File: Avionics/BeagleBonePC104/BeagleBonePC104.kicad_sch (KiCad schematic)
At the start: 5 parts

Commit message: Ian Goldberg - Finished the footprint for the BeagleBonePCI104 Motherboard
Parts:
- removed U2: ~, symbol PCI104:PCI104Connector
- removed U3: ~, AdafruitCANTransciever:AdafruitCANPal_TJA1051T, symbol BeagleBoneBlackPinout:AdafruitCANTransciever
- added U2: ~, PCI104Connector:PCI104ConnectorAttempt#2H1, symbol PCI104:PCI104H1
- added U3: ~, AdafruitCANTransciever:AdafruitCANPal_TJA1051T, symbol BeagleBoneBlackPinout:AdafruitCANTranscieverAttempt#2
- added U4: ~, PCI104Connector:PCI104ConnectorAttempt#2H2, symbol PCI104:PCI104H2
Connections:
- net GPIO3_21 is gone; now on net CAN_SLNT: U1.25 (GPIO3_21)
- net 3V3: now also U2.25 (3V3_MAIN), U2.26 (3V3_MAIN), U3.1 (Vcc), U4.27 (3V3_MAIN), U4.28 (3V3_MAIN)
- net 5V: now also U4.25 (5V_MAIN), U4.26 (5V_MAIN)
- net CAN1_RX: now also U3.4 (TX)
- net CAN1_TX: now also U3.3 (RX)
- net CAN_H: now also U2.3 (CANH1), U3.6 (CANH)
- net CAN_L: now also U2.1 (CANL1), U3.7 (CANL)
- net GND: now also U3.2 (GND), U4.29 (GND), U4.30 (GND), U4.31 (GND), U4.32 (GND)
- net GPI02_22: now also U2.29
- net GPIO0_7: now also U4.19
- net GPIO1_12: now also U2.13
- net GPIO1_13: now also U2.11
- net GPIO1_14: now also U4.17
- net GPIO1_15: now also U2.17
- net GPIO1_16: now also U4.40
- net GPIO1_17: now also U4.44
- net GPIO1_26: now also U2.15
- net GPIO1_27: now also U2.21
- net GPIO1_28: now also U4.43
- net GPIO1_29: now also U2.27
- net GPIO2_1: now also U2.23
- net GPIO2_10: now also U2.24
- net GPIO2_11: now also U2.28
- net GPIO2_12: now also U2.44
- net GPIO2_13: now also U2.22
- net GPIO2_23: now also U2.46
- net GPIO2_24: now also U2.45
- net GPIO2_25: now also U2.42
- net GPIO2_6: now also U2.36
- net GPIO2_7: now also U4.16
- net GPIO2_8: now also U2.30
- net GPIO2_9: now also U2.34
- net GPIO3_19: now also U4.22
- net GPIO3_20: now also U4.21
- net I2C_SCL: now also U2.43 (I2C1_SCL)
- net I2C_SDA: now also U2.41 (I2C1_SDA)
- net SYS_RESETn: now also U2.12 (BGLBON_RST)
- net UART_RX: now also U2.35 (GNSS_UART_RX)
- net UART_TX: now also U2.33 (GNSS_UART_TX)
- net CAN_SLNT: now reaches U1.25 (GPIO3_21)
- net CAN_SLNT: now also U3.5 (SLNT)
- new net CAN_SNLT: U4.50

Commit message: Finally finished the BeagleBone Motherboard
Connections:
- no-connect marks 107 -> 109
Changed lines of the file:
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@@
 	)
 	(junction
-		(at 93.98 74.93)
-		(diameter 0)
-		(color 0 0 0 0)
-	)
-	(junction
 		(at 74.93 115.57)
 		(diameter 0)
@@
 		(color 0 0 0 0)
 	)
+	(junction
+		(at 93.98 74.93)
+		(diameter 0)
+		(color 0 0 0 0)
+	)
 	(no_connect
 		(at 93.98 143.51)
@@
 	)
 	(no_connect
+		(at 326.39 149.86)
+	)
+	(no_connect
 		(at 93.98 90.17)
 	)
@@
 	)
 	(no_connect
+		(at 326.39 152.4)
+	)
+	(no_connect
 		(at 240.03 106.68)
 	)
@@
 	(wire
 		(pts
+			(xy 64.77 74.93) (xy 93.98 74.93)
+		)
+		(stroke
+			(width 0)
+			(type default)
+		)
+	)
+	(wire
+		(pts
 			(xy 278.13 144.78) (xy 284.48 144.78)
 		)
@@
 	(wire
 		(pts
-			(xy 64.77 74.93) (xy 93.98 74.93)
-		)
-		(stroke
-			(width 0)
-			(type default)
-		)
-	)
-	(wire
-		(pts
 			(xy 278.13 152.4) (xy 284.48 152.4)
 		)
@@
 	(wire
 		(pts
+			(xy 64.77 77.47) (xy 64.77 74.93)
+		)
+		(stroke
+			(width 0)
+			(type default)
+		)
+	)
+	(wire
+		(pts
 			(xy 93.98 184.15) (xy 93.98 186.69)
 		)
@@
 		)
 	)
+	(netclass_flag ""
+		(length 2.54)
+		(shape round)
+		(at 69.85 74.93 0)
+		(fields_autoplaced yes)
+		(effects
+			(font
+				(size 1.27 1.27)
+			)
+			(justify left bottom)
+		)
+		(property "Netclass" "Power"
+			(at 70.5485 72.39 0)
+			(effects
+				(font
+					(size 1.27 1.27)
+					(italic yes)
+				)
+				(justify left)
+				(hide yes)
+			)
+		)
+	)
+	(netclass_flag ""
+		(length 2.54)
+		(shape round)
+		(at 93.98 190.5 90)
+		(fields_autoplaced yes)
+		(effects
+			(font
+				(size 1.27 1.27)
+			)
+			(justify left bottom)
+		)
+		(property "Netclass" "Power"
+			(at 91.44 189.8015 90)
+			(effects
+				(font
+					(size 1.27 1.27)
+					(italic yes)
+				)
+				(justify left)
+				(hide yes)
+			)
+		)
+	)
+	(netclass_flag ""
+		(length 2.54)
+		(shape round)
+		(at 163.83 74.93 0)
+		(fields_autoplaced yes)
+		(effects
+			(font
+				(size 1.27 1.27)
+			)
+			(justify left bottom)
+		)
+		(property "Netclass" "Power"
+			(at 164.5285 72.39 0)
+			(effects
+				(font
+					(size 1.27 1.27)
+					(italic yes)
+				)
+				(justify left)
+				(hide yes)
+			)
+		)
+	)
 	(symbol
 		(lib_id "Device:R")
@@
 	(symbol
 		(lib_id "power:GND")
-		(at 64.77 74.93 0)
+		(at 64.77 77.47 0)
 		(unit 1)
 		(exclude_from_sim no)
@@
 		(fields_autoplaced yes)
 		(property "Reference" "#PWR03"
-			(at 64.77 81.28 0)
+			(at 64.77 83.82 0)
 			(effects
 				(font
@@
 		)
 		(property "Value" "GND"
-			(at 64.77 80.01 0)
+			(at 64.77 82.55 0)
 			(effects
 				(font
@@
 		)
 		(property "Footprint" ""
-			(at 64.77 74.93 0)
+			(at 64.77 77.47 0)
 			(effects
 				(font
@@
 		)
 		(property "Datasheet" ""
-			(at 64.77 74.93 0)
+			(at 64.77 77.47 0)
 			(effects
 				(font
@@
 		)
 		(property "Description" "Power symbol creates a global label with name \"GND\" , ground"
-			(at 64.77 74.93 0)
+			(at 64.77 77.47 0)
 			(effects
 				(font

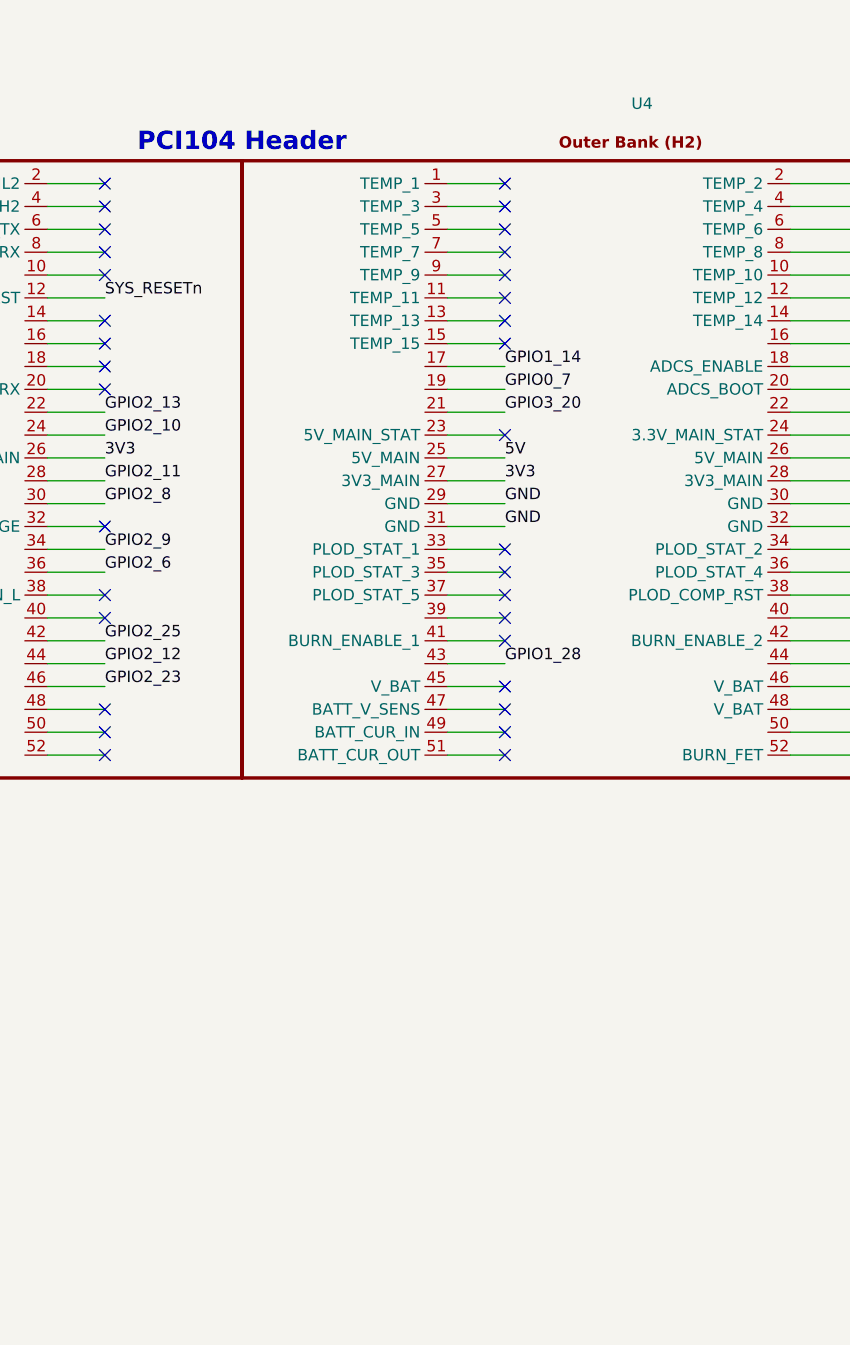
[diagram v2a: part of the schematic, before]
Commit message: Ian Goldberg - Finished Version 2 of the flight computer, added a temperature sensor to the board.
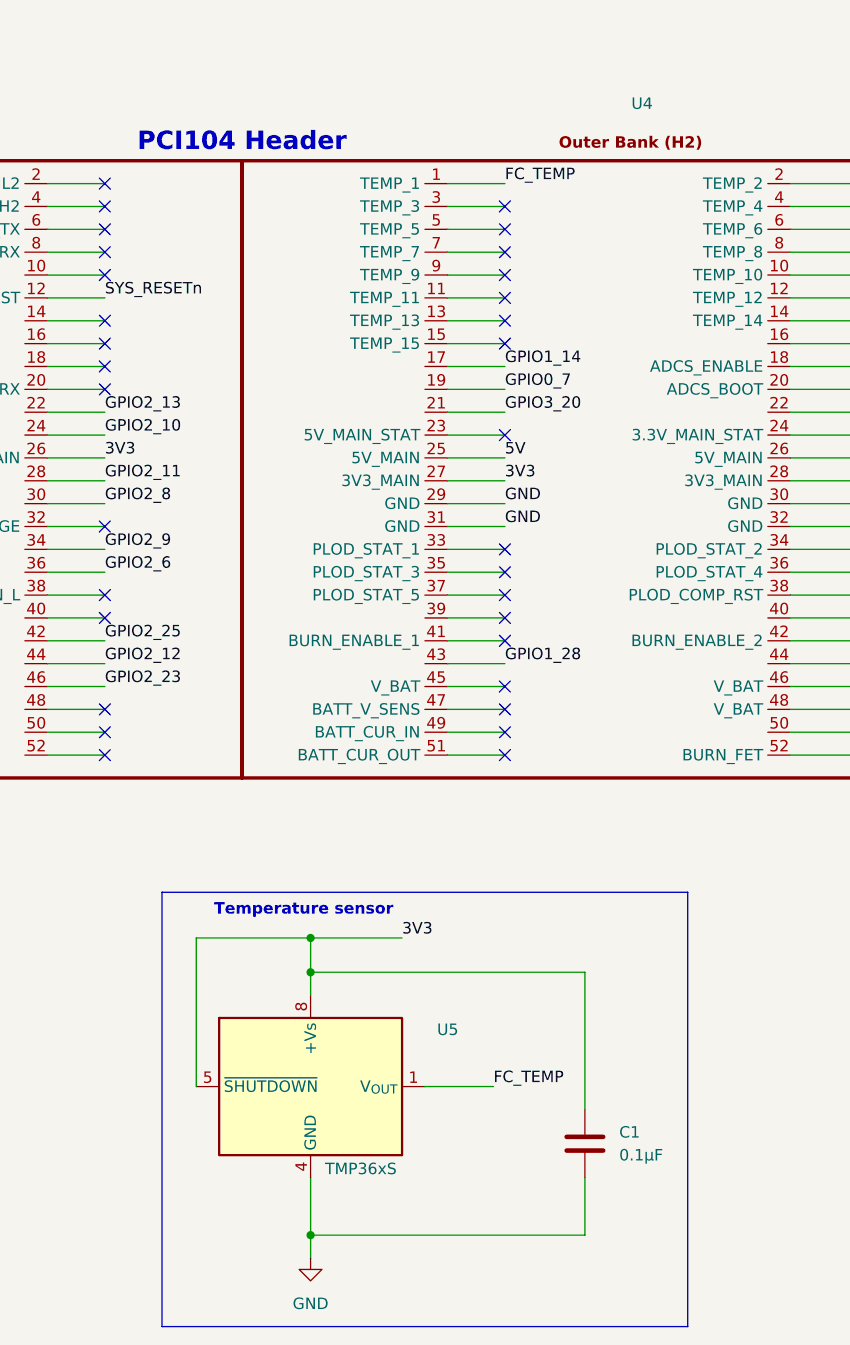
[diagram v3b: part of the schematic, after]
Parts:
- added C1: 0.1µF, Capacitor_SMD:C_0805_2012Metric, symbol Device:C
- added U5: TMP36xS, Package_SO:SOIC-8_3.9x4.9mm_P1.27mm, symbol Sensor_Temperature:TMP36xS
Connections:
- net 3V3: now also C1.1, U5.5 (~{SHUTDOWN}), U5.8 (+Vs)
- net GND: now also C1.2, U5.4 (GND)
- net FC_TEMP: now reaches U4.1 (TEMP_1)
- net FC_TEMP: now also U5.1 (V_{OUT})
- no-connect marks 109 -> 108
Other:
- note added: "Temperature sensor"

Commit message: Ian Goldberg - Finished the second version of the flight computer board
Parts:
- added D1: 5V Status, LED_SMD:LED_0805_2012Metric, symbol Device:LED
- added D2: 3V3 Status, LED_SMD:LED_0805_2012Metric, symbol Device:LED
- added D3: Beaglebone Ready, LED_SMD:LED_0805_2012Metric, symbol Device:LED
- added R3, R4, R5: 15, Resistor_SMD:R_0805_2012Metric, symbol Device:R
- R1, R2: value 10k -> 5.6k
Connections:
- net 3V3: now also R3.1
- net 5V: now also R4.1
- net GND: now also D1.1 (K), D2.1 (K), D3.1 (K)
- net SYS_RESETn: now also R5.1
- new net: D3.2 (A), R5.2
- new net: D1.2 (A), R3.2
- new net: D2.2 (A), R4.2
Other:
- note added: "LED: LSM0805463V Resistor: RMCF0805FT15R0"
- note added: "Status LED indicators"
- moved on the sheet: C1, U5
